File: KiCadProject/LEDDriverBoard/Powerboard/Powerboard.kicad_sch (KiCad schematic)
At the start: 28 parts, among them J1 XT30, J2 XT30, J3 Conn_01x03_Male, Q1 Q_NMOS_GDS, Q2 SUD50P10-43L-GE3, U1 MAX16833

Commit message: BQ25713 and LDO done? Stm32 next I think
Signed-off-by: Eldalote.Electronics <Eldalote.Electronics@gmail.com>
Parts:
- C1: symbol Device:C_Small -> Device:C_Polarized_Small
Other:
- note added: "Connector cap (system output cap from battery charger)"
- note removed: "Connector cap"
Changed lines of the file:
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@@
     (effects (font (size 0.8 0.8)) (justify left bottom))
   )
-  (text "Connector cap" (at 44.45 73.66 0)
+  (text "Connector cap \n(system output cap from \nbattery charger)\n"
+    (at 49.53 71.12 0)
     (effects (font (size 1.27 1.27)) (justify left bottom))
   )
@@
     (pin "1")
   )
-  (symbol (lib_id "Device:C_Small") (at 43.18 67.31 0) (unit 1)
+  (symbol (lib_id "Device:C_Polarized_Small") (at 43.18 67.31 0) (unit 1)
     (in_bom yes) (on_board yes)
     (property "Reference" "C1" (id 0) (at 45.72 66.0462 0)

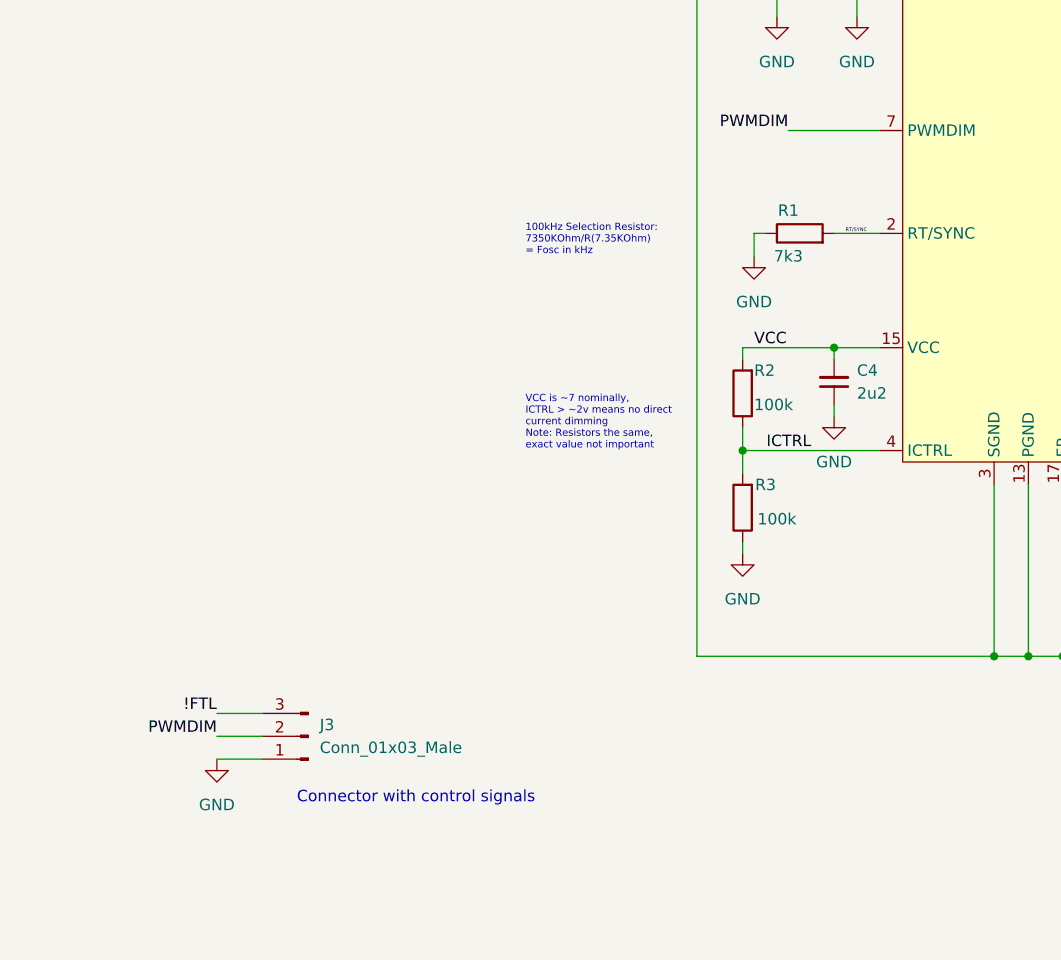
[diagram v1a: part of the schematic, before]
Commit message: Final touches before component order and PCB layout
Signed-off-by: Eldalote.Electronics <Eldalote.Electronics@gmail.com>
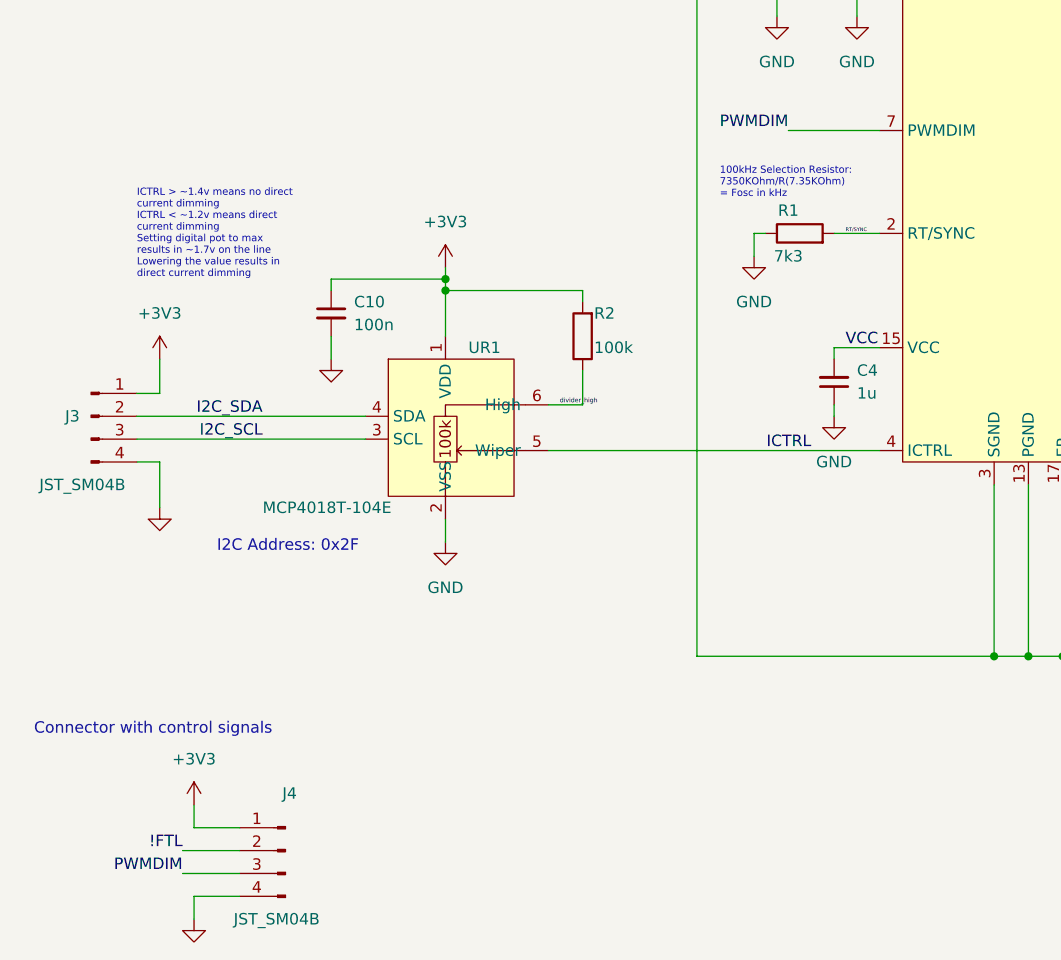
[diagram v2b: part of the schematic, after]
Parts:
- removed J3: Conn_01x03_Male, Connector_PinHeader_2.54mm:PinHeader_1x03_P2.54mm_Vertical, symbol Connector:Conn_01x03_Male
- removed R3: 100k, Resistor_SMD:R_0402_1005Metric, symbol Device:R
- added C10: 100n, Capacitor_SMD:C_0402_1005Metric, symbol Device:C_Small
- added J3, J4: JST_SM04B, Connector_JST:JST_SH_SM04B-SRSS-TB_1x04-1MP_P1.00mm_Horizontal, symbol Connector:Conn_01x04_Male
- added UR1: MCP4018T-104E, Package_TO_SOT_SMD:SOT-363_SC-70-6, symbol Eldalote_symbols:MCP4018T-104E
- C4: value 2u2 -> 1u
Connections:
- net !FTL: now also J4.2 (Pin_2)
- net GND: now also C10.2, J3.4 (Pin_4), J4.4 (Pin_4), UR1.2 (VSS)
- net ICTRL: now also UR1.5 (Wiper); no longer R2.1
- net PWMDIM: now also J4.3 (Pin_3)
- net VCC: no longer R2.2
- new net +3V3: C10.1, J3.1 (Pin_1), J4.1 (Pin_1), R2.2, UR1.1 (VDD)
- new net I2C_SCL: J3.3 (Pin_3), UR1.3 (SCL)
- new net I2C_SDA: J3.2 (Pin_2), UR1.4 (SDA)
- new net divider_high: R2.1, UR1.6 (High)
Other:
- note added: "I2C Address: 0x2F"
- note added: "ICTRL > ~1.4v means no direct current dimming ICTRL < ~1.2v means direct current dimming Setting digital pot to max results in ~1.7v on the line Lowering the value results in direct current dimming"
- note removed: "VCC is ~7 nominally, ICTRL > ~2v means no direct current dimming Note: Resistors the same, exact value not important"

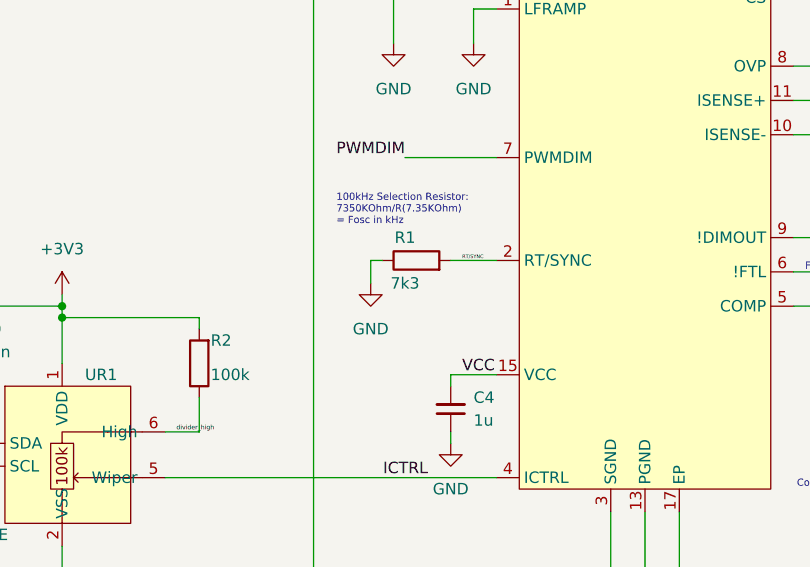
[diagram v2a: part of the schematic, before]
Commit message: Components selected, MfID added to schematics, and components ordered
Signed-off-by: Eldalote.Electronics <Eldalote.Electronics@gmail.com>
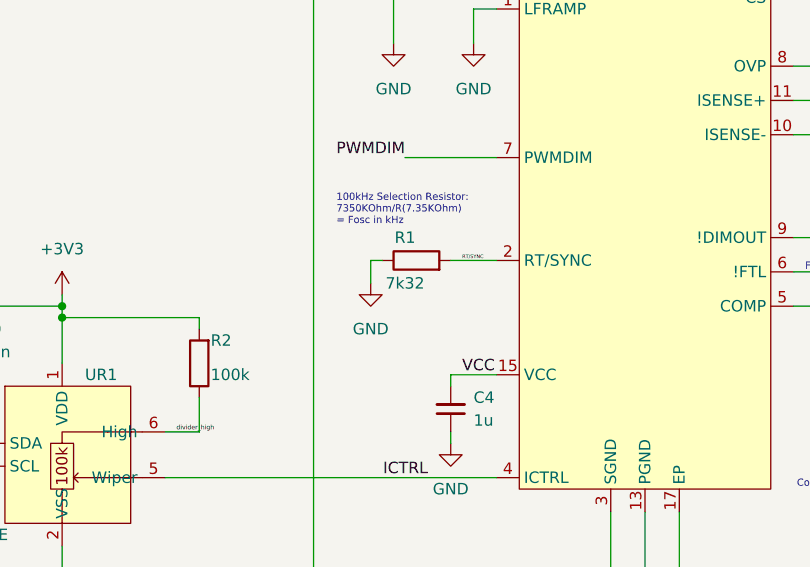
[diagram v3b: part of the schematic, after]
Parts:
- C1: Extra requirement (none) -> 35V; MfID (none) -> 865080542006
- C10: MfID (none) -> CL05A104KA5NNNC
- C2: Extra requirement (none) -> 50V; MfID (none) -> CL31B106KBHNNNE
- C3: footprint Capacitor_SMD:C_0402_1005Metric -> Capacitor_SMD:C_0603_1608Metric; Extra requirement (none) -> 50V; MfID (none) -> CL10B104KB8NNWC
- C4: Extra requirement (none) -> 16V; MfID (none) -> CL05A105KO5NNNC
- C5: Alt MfID (none) -> GCJ188R91E394KA01D; Extra requirement (none) -> 25V; MfID (none) -> TMK107B7224KA-T
- C6, C7, C8, C9: Extra requirement (none) -> 100V; MfID (none) -> GRJ31CC72A475KE01L
- D1: Extra requirement (none) -> 100v 5A; MfID (none) -> SDT5H100P5-7
- J3, J4: MfID (none) -> SM04B-SRSS-TB(LF)(SN)
- L1: Extra requirement (none) -> 8.4A av. 9.6A peak; MfID (none) -> SRP1265C-6R8M
- Q1: Extra requirement (none) -> 90V 5A; MfID (none) -> AOD66920
- Q2: Extra requirement (none) -> 90V 5A; MfID (none) -> SUD50P10-43L-GE3
- R1: value 7k3 -> 7k32; MfID (none) -> RC0402FR-077K32L
- R10, R2: MfID (none) -> CR0402-FX-1003GLF
- R4: Alt MfID (none) -> RMCF0402FT2K70; MfID (none) -> CR0402-FX-4701GLF
- R5: Alt MfID (none) -> RC0603FR-074M75L; MfID (none) -> RC0603FR-075M1L
- R6: Alt MfID (none) -> CSR1206FTR130; Extra requirement (none) -> min 1/2 watt rating; MfID (none) -> KDV12FR330ET
- R7: footprint Resistor_SMD:R_0603_1608Metric -> Resistor_SMD:R_0805_2012Metric; MfID (none) -> RK73H2ATTD1000F
- R8: Alt MfID (none) -> CR0402-FX-1200GLF; MfID (none) -> RC0402FR-07910RL
- R9: Alt MfID (none) -> D1WEL1206MR033FA-T5; MfID (none) -> RL1206FR-7W0R051L
- U1: MfID (none) -> MAX16833AUE+
- UR1: MfID (none) -> MCP4018T-104E/LT
